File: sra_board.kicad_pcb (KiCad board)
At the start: 2 copper layers, 90 x 89.5 mm, 168 parts, among them J1 Conn_01x14_Pin, J10 Conn_01x03_Pin, J11 Conn_01x03_Pin, J12 Conn_01x03_Pin, J13 MPU0650, J14 LSA, J15 OLED, J16 Conn_01x03_Pin, J17 Conn_01x03_Pin, J18 Conn_01x03_Pin, J3 Conn_01x08_Pin, J4 Conn_01x14_Pin, J5 USB_C_Receptacle_USB2.0_16P, J6 B2B-XH-A_LF__SN_, J7 B2B-XH-A_LF__SN_, J8 B2B-XH-A_LF__SN_, J9 Conn_01x03_Pin, Q1 SS8050, Q2 SS8050, Q3 AO3400A, Q4 AO3401A, Q5 AO3401A, Q6 AO3401A, Q7 AO3401A, SW1 SW_0, SW2 SW_EN, SW3 Switch, SW4 Switch, SW5 SW_Wuerth_450301014042, SW6 SW_Wuerth_450301014042, U1 MAX7219CWG_T, U2 CH340C, U3 TB6612FNG H-bridge Motor Driv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, U5 CN3303, U6 TPS562202, U7 ME6211C33M5, U8 ESP32-WROOM-32E

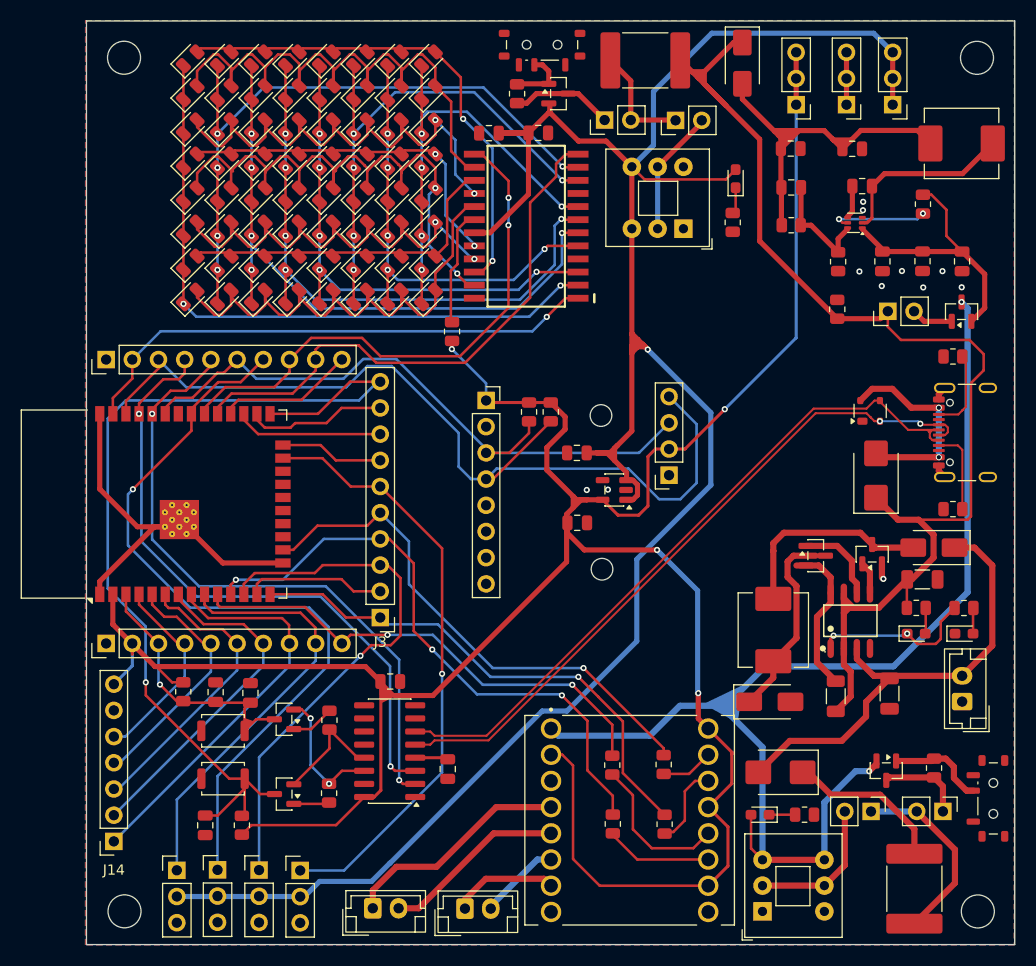
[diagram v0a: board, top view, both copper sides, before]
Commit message: Changing the buck converter IC and adding silkscreen and increasing thickness of traces
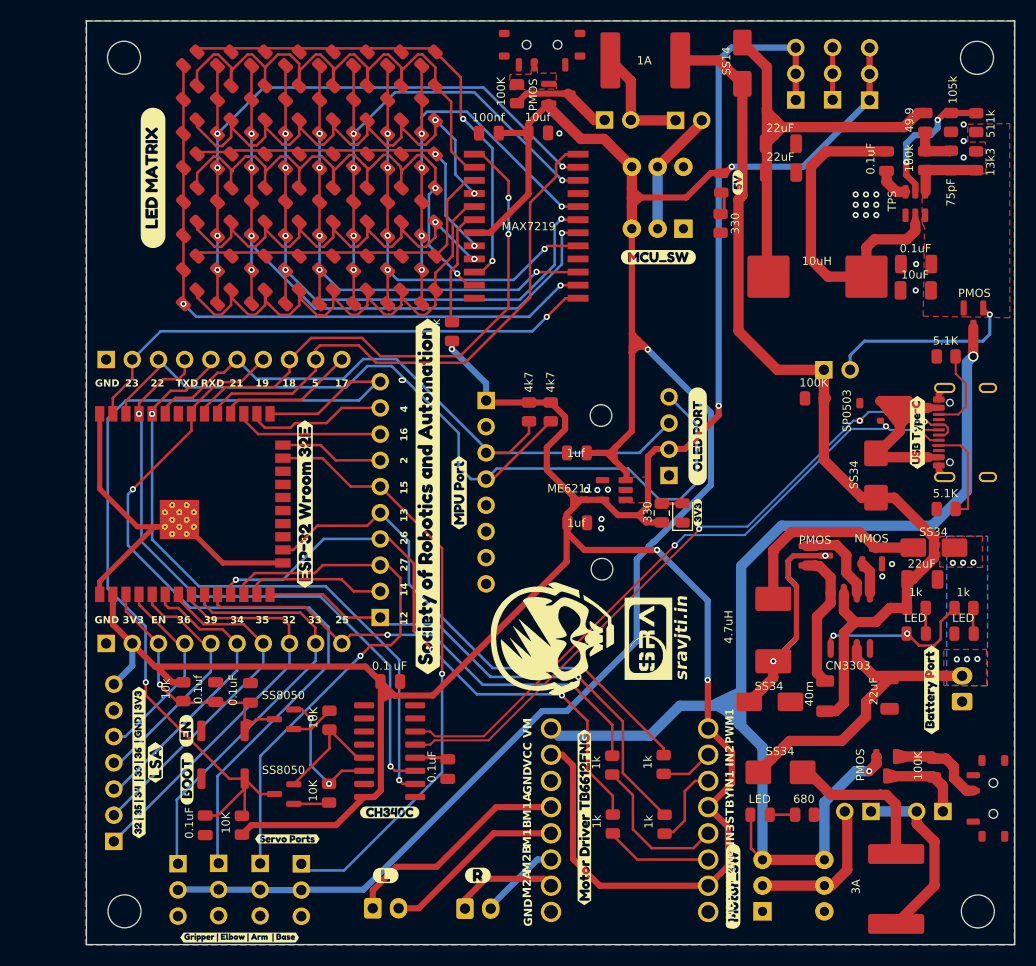
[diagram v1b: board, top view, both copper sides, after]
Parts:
- removed C12: 10uF, Capacitor_SMD:C_0805_2012Metric
- removed C13, C14: 22uF, Capacitor_SMD:C_0805_2012Metric
- removed C15: NC, Capacitor_SMD:C_0805_2012Metric
- removed U6: TPS562202, Package_TO_SOT_SMD:SOT-563
- added 330: 330, Resistor_SMD:R_0805_2012Metric, F.Cu at (170.1, 97.6)
- added C20: 22uF, Capacitor_SMD:C_1206_3216Metric, F.Cu at (181.7, 61.8)
- added C21: 22uF, Capacitor_SMD:C_1206_3216Metric, F.Cu at (181.7, 64.6)
- added C22: 75pF, Capacitor_SMD:C_0805_2012Metric, F.Cu at (198.1, 63.4)
- added D77: LED, LED_SMD:LED_0805_2012Metric, F.Cu at (172.1, 97.6)
- added G***: LOGO, logos:sra_logo_small_neg, F.Cu at (168.8, 109.8)
- added G***: LOGO, logos:sra_skull_big, F.Cu at (159.5, 109.7)
- added G***: LOGO, Logos:sra_logo_big, B.Cu at (123.0, 68.8)
- added G***: LOGO, logos:sra_board_github_qr_code, B.Cu at (156.0, 71.8)
- added G***: LOGO, logos:sra_skull_big, B.Cu at (159.2, 110.2)
- added G***: LOGO, logos:espressif_logo, B.Cu at (122.1, 96.5)
- added R16: 100k, Resistor_SMD:R_0805_2012Metric, F.Cu at (195.6, 63.5)
- added R25: 13k3, Resistor_SMD:R_0805_2012Metric, F.Cu at (200.6, 63.5)
- added U4: TPS54302, Package_TO_SOT_SMD:SOT-23-6, F.Cu at (194.7, 67.6)
- added kibuzzard-658F2C3C: G***, kibuzzard-658F2C3C, F.Cu at (121.0, 121.8)
- added kibuzzard-668D4F81: G***, kibuzzard-668D4F81, F.Cu at (150.5, 95.7)
- added kibuzzard-668FE423: G***, kibuzzard-668FE423, F.Cu at (194.9, 89.8)
- added kibuzzard-668FF9B2: G***, kibuzzard-668FF9B2, F.Cu at (173.6, 90.2)
- added kibuzzard-66914CE9: G***, kibuzzard-66914CE9, B.Cu at (130.2, 96.5)
- added kibuzzard-66921043: G***, kibuzzard-66921043, B.Cu at (128.2, 96.3)
- added kibuzzard-66923428: G***, kibuzzard-66923428, F.Cu at (162.6, 127.1)
- added kibuzzard-66CD8CDE: G***, kibuzzard-66CD8CDE, F.Cu at (129.2, 138.8)
- added kibuzzard-66CD901B: G***, kibuzzard-66CD901B, F.Cu at (133.8, 129.2)
- added kibuzzard-66CF86D1: G***, kibuzzard-66CF86D1, F.Cu at (177.0, 133.8)
- added kibuzzard-66CF86E5: G***, kibuzzard-66CF86E5, F.Cu at (169.8, 72.8)
- added kibuzzard-66D06403: G***, kibuzzard-66D06403, F.Cu at (135.5, 96.8)
- added kibuzzard-66D06F4C: G***, kibuzzard-66D06F4C, F.Cu at (124.1, 123.4)
- added kibuzzard-66D06F54: G***, kibuzzard-66D06F54, F.Cu at (124.0, 118.7)
- added kibuzzard-66D58886: G***, kibuzzard-66D58886, F.Cu at (173.6, 97.6)
- added kibuzzard-675FD791: G***, kibuzzard-675FD791, F.Cu at (143.7, 126.6)
- added kibuzzard-675FDA6A: G***, kibuzzard-675FDA6A, F.Cu at (147.4, 96.0)
- added kibuzzard-675FF2F7: G***, kibuzzard-675FF2F7, F.Cu at (196.3, 114.8)
- added kibuzzard-675FF39E: G***, kibuzzard-675FF39E, F.Cu at (119.4, 121.8)
- added kibuzzard-6774F4AA: G***, kibuzzard-6774F4AA, F.Cu at (152.3, 132.8)
- added kibuzzard-6774F4AE: G***, kibuzzard-6774F4AE, F.Cu at (143.3, 132.8)
- added kibuzzard-67A02922: G***, kibuzzard-67A02922, F.Cu at (177.5, 65.6)
- added kibuzzard-68E7F907: G***, kibuzzard-68E7F907, F.Cu at (120.8, 65.1)
- C10, C11: footprint Capacitor_SMD:C_0805_2012Metric -> Capacitor_SMD:C_1206_3216Metric
- D1: value SP0503BAHT -> SP0503
- D67, D69, D74, D76: footprint LED_SMD:LED_0603_1608Metric_Pad1.05x0.95mm_HandSolder -> LED_SMD:LED_0805_2012Metric
- L2: value 4.7uH -> 10uH; footprint Inductor_SMD:L_Sunlord_MWSA0603S -> Inductor_SMD:L_Sunlord_MWSA1004S
- R17: value 10k -> 511k
- R18: value 10k -> 49.9
- R19: value 52k3 -> 105k
- R21, R22: value R -> 4k7
- moved L2 19.0 mm to (185.2, 74.7)
- moved R19 18.4 mm to (198.1, 59.7), turned to 90 degrees
- moved R18 15.9 mm to (195.7, 59.7), turned to -90 degrees
- moved R17 9.44 mm to (200.6, 59.8)
- moved R1 8.92 mm to (184.9, 86.5), turned to 180 degrees
- moved JP1 8.40 mm to (185.8, 83.7)
- moved C16 3.38 mm to (191.9, 63.5), turned to 90 degrees
- moved C10 3.28 mm to (194.8, 73.5), turned to 180 degrees
- moved C11 2.90 mm to (194.7, 76.0), turned to 180 degrees
- moved J16 2.28 mm to (190.3, 57.6)
- moved F1 1.77 mm to (192.8, 134.1)
- moved D76 1.45 mm to (175.9, 65.6)
- moved J18 1.42 mm to (186.7, 57.6)
- moved Q5 1.29 mm to (200.3, 78.7), turned to -90 degrees
- moved R20 1.18 mm to (175.8, 69.5)
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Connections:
- C16 pad 1: Net-(U6-SW) -> Net-(U4-BOOT)
- C16 pad 2: Net-(U6-VBST) -> Net-(U4-SW)
- L2 pad 1: Net-(U6-SW) -> Net-(U4-SW)
- R17 pad 1: /VTPS -> Net-(U4-EN)
- R17 pad 2: Net-(U6-EN) -> /VTPS
- R18 pad 1: GND -> +5V
- R18 pad 2: Net-(U6-VFB) -> Net-(C22-Pad1)
- R19 pad 1: +5V -> GND
- R19 pad 2: Net-(U6-VFB) -> Net-(U4-EN)
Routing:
- net /5V_P_USB: track 124.1 -> 90.1 mm
- net Net-(U4-SW): track 0.00 -> 31.9 mm
- net /VTPS: track 26.3 -> 0.00 mm
- net /5V_P: track 218.7 -> 197.7 mm, vias 1 -> 2
- net Net-(U6-SW): track 16.7 -> 0.00 mm
- net +BATT: track 45.5 -> 29.2 mm, vias 0 -> 6
- net Net-(D68-K): track 18.8 -> 34.5 mm, vias 0 -> 2
- net Net-(JP1-B): track 4.06 -> 18.6 mm, vias 0 -> 1
- net Net-(U4-EN): track 0.00 -> 13.5 mm, vias 0 -> 2
- net Net-(U6-VFB): track 11.0 -> 0.00 mm
- net /3V3: track 256.3 -> 266.9 mm
- net Net-(U6-EN): track 9.35 -> 0.00 mm, vias 2 -> 0
- net +5V: track 36.6 -> 44.5 mm
- net Net-(U4-FB): track 0.00 -> 7.08 mm
- net Net-(Q7-G): track 5.91 -> 0.00 mm
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- added copper zone on B.Cu, net +BATT
- added copper zone on F.Cu, net +BATT
- added copper zone on F.Cu, net /5V_P
- added copper zone on F.Cu, net /VTPS
- added copper zone on F.Cu, net Net-(Q7-G)
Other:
- board text added: "0"
- board text added: "0.1 uF"
- board text added: "0.1uF"
- board text added: "0.1uf"
- board text added: "100K"
- board text added: "100k"
- board text added: "100nf"
- board text added: "105k"
- board text added: "10K"
- board text added: "10k"
- board text added: "10uF"
- board text added: "10uH"
- board text added: "10uf"
- board text added: "12"
- board text added: "13"
- board text added: "13k3"
- board text added: "14"
- board text added: "15"
- board text added: "16"
- board text added: "17"
- board text added: "18"
- board text added: "19"
- board text added: "1A"
- board text added: "1k"
- board text added: "1uf"
- board text added: "2"
- board text added: "21"
- board text added: "22"
- board text added: "22uF"
- board text added: "23"
- board text added: "25"
- board text added: "26"
- board text added: "27"
- board text added: "32"
- board text added: "33"
- board text added: "330"
- board text added: "34"
- board text added: "35"
- board text added: "36"
- board text added: "39"
- board text added: "3A"
- board text added: "4"
- board text added: "4.7uH"
- board text added: "40m"
- board text added: "49.9"
- board text added: "4k7"
- board text added: "5"
- board text added: "5.1K"
- board text added: "511k"
- board text added: "680"
- board text added: "75pF"
- board text added: "CN3303"
- board text added: "EN"
- board text added: "GND"
- board text added: "GND 3V3"
- board text added: "IN1"
- board text added: "IN2"
- board text added: "IN3"
- board text added: "IN4"
- board text added: "LED"
- board text added: "M1A"
- board text added: "M1B"
- board text added: "M2A"
- board text added: "M2B"
- board text added: "MAX7219"
- board text added: "ME6211"
- board text added: "NMOS"
- board text added: "PCB Edge"
- board text added: "PMOS"
- board text added: "PWM1"
- board text added: "PWM2"
- board text added: "RXD"
- board text added: "SP0503"
- board text added: "SS14"
- board text added: "SS34"
- board text added: "SS8050"
- board text added: "STBY"
- board text added: "TPS"
- board text added: "TXD"
- board text added: "VCC"
- board text added: "VM"
- board text added: "sravjti.in"
